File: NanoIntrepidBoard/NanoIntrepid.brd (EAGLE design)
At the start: 35 x 50 mm, 22 parts, among them Q1 TRANS_NPN, Q2 TRANS_NPN, Q3 TRANS_NPN, Q4 TRANS_PNP, Q5 TRANS_PNP, Q6 TRANS_PNP, U1 NANO, U2 MOSFET_P, U3 MOSFET_P, U4 MOSFET_P

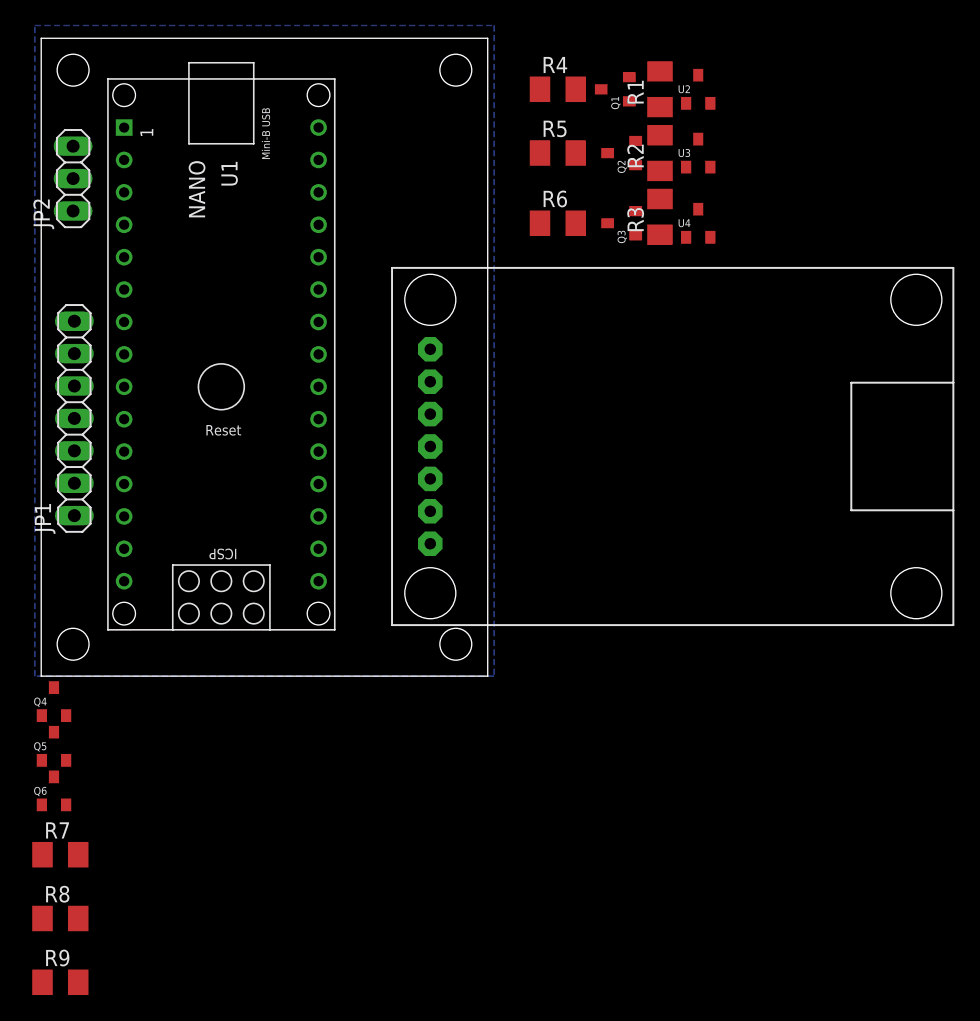
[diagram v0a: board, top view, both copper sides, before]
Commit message: Fixed some Eagle Library mistakes and started laying out board
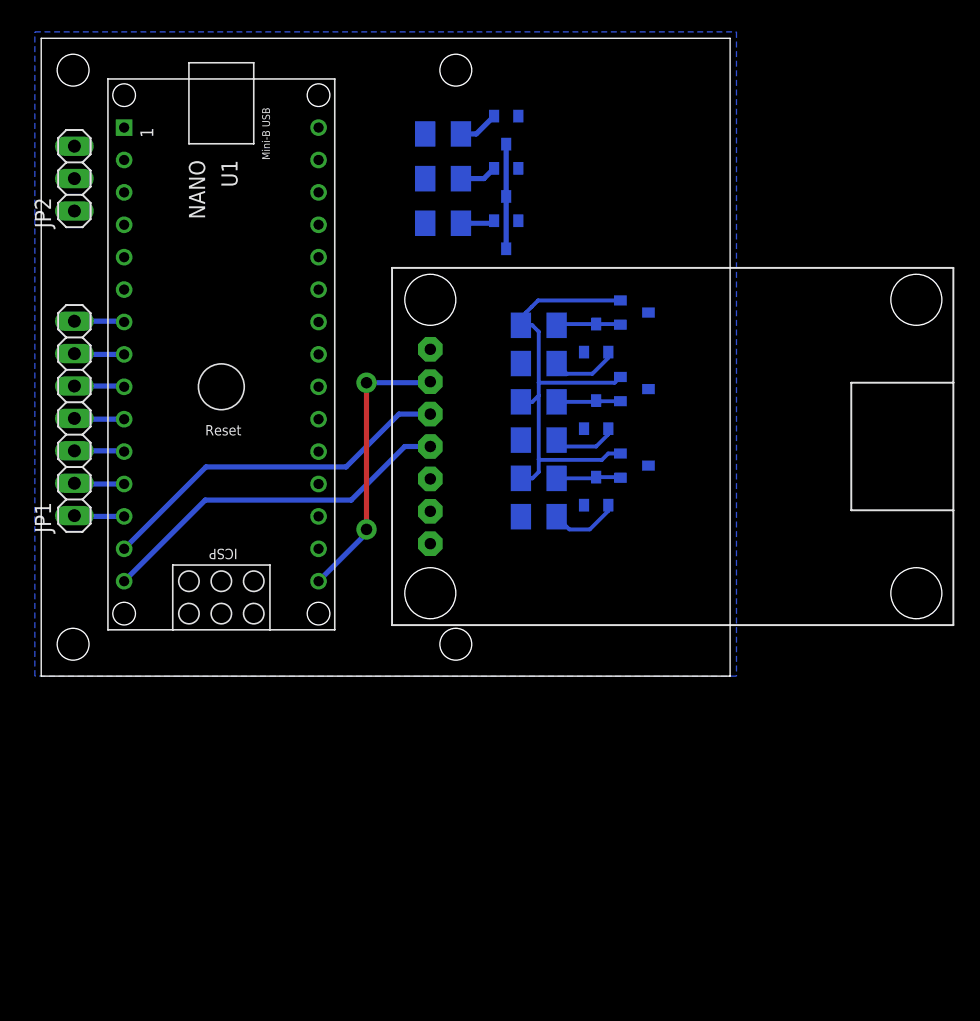
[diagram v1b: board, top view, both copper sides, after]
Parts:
- moved R9 66.6 mm to (31.5, 35.5), flipped to the bottom, turned to 180 degrees
- moved R8 65.3 mm to (31.5, 39.0), flipped to the bottom, turned to 180 degrees
- moved R7 64.0 mm to (31.5, 42.5), flipped to the bottom, turned to 180 degrees
- moved Q4 55.6 mm to (36.5, 41.8), flipped to the bottom, turned to 180 degrees
- moved Q5 55.1 mm to (36.5, 37.7), flipped to the bottom, turned to 180 degrees
- moved Q6 54.7 mm to (36.5, 33.6), flipped to the bottom, turned to 180 degrees
- moved R6 23.0 mm to (39.0, 12.5), flipped to the bottom, turned to 180 degrees
- moved R3 22.6 mm to (39.0, 15.5), flipped to the bottom, turned to 0 degrees
- moved R5 22.5 mm to (39.0, 18.5), flipped to the bottom, turned to 180 degrees
- moved R2 21.7 mm to (39.0, 21.5), flipped to the bottom, turned to 0 degrees
- moved R4 21.6 mm to (39.0, 24.5), flipped to the bottom, turned to 180 degrees
- moved R1 20.8 mm to (39.0, 27.5), flipped to the bottom, turned to 0 degrees
- moved U4 20.4 mm to (47.5, 16.5), flipped to the bottom, turned to 90 degrees
- moved Q3 20.0 mm to (43.5, 15.5), flipped to the bottom, turned to 0 degrees
- moved U3 19.9 mm to (47.5, 22.5), flipped to the bottom, turned to 90 degrees
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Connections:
- net +12V: now also U2.2, U3.2, U4.2; no longer U2.1, U3.1, U4.1
- net N$13: now also U2.1; no longer U2.2
- net N$14: now also U3.1; no longer U3.2
- net N$16: now also U4.1; no longer U4.2
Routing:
- net +12V: track 0.00 -> 38.1 mm
- net N$2: track 0.00 -> 28.4 mm
- net N$3: track 0.00 -> 28.4 mm
- net N$1: track 0.00 -> 22.2 mm, vias 0 -> 2
- net +5V: track 0.00 -> 8.20 mm
- net N$17: track 0.00 -> 5.51 mm
- net N$12: track 0.00 -> 5.35 mm
- net N$11: track 0.00 -> 5.10 mm
- net N$14: track 0.00 -> 5.09 mm
- net N$13: track 0.00 -> 5.06 mm
- net N$16: track 0.00 -> 5.06 mm
- net N$5: track 0.00 -> 3.92 mm
- net N$10: track 0.00 -> 3.92 mm
- net N$8: track 0.00 -> 3.92 mm
- net N$6: track 0.00 -> 3.92 mm
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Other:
- board size 35 x 50 mm -> 54 x 50 mm

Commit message: Worked on board files
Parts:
- added JP3: (no value), pinhead:1X01
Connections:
- new net ABS_UC: R8.1, U1.23
- new net AIRBAG_UC: R7.1, U1.24
- new net HB_UC: R4.1, U1.21
- new net LTURN_UC: R6.1, U1.19
- new net OIL_UC: R9.1, U1.22
- new net PB: JP3.1, U1.6
- new net RTURN_UC: R5.1, U1.20
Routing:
- net LTURN_UC: track 0.00 -> 43.7 mm, vias 0 -> 2
- net HB_UC: track 0.00 -> 20.6 mm
- net AIRBAG_UC: track 0.00 -> 20.0 mm
- net ABS_UC: track 0.00 -> 19.4 mm
- net RTURN_UC: track 0.00 -> 19.1 mm
- net OIL_UC: track 0.00 -> 16.9 mm
- net PB: track 0.00 -> 4.60 mm
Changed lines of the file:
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@@
 <?xml version="1.0" encoding="utf-8"?>
 <!DOCTYPE eagle SYSTEM "eagle.dtd">
-<eagle version="9.6.2">
+<eagle version="7.5.0">
 <drawing>
 <settings>
 <setting alwaysvectorfont="no"/>
-<setting keepoldvectorfont="yes"/>
 <setting verticaltext="up"/>
 </settings>
@@
 <param name="dpMaxLengthDifference" value="10mm"/>
 <param name="dpGapFactor" value="2.5"/>
+<param name="checkGrid" value="0"/>
 <param name="checkAngle" value="0"/>
 <param name="checkFont" value="1"/>
 <param name="checkRestrict" value="1"/>
-<param name="checkStop" value="0"/>
-<param name="checkValues" value="0"/>
-<param name="checkNames" value="1"/>
-<param name="checkWireStubs" value="1"/>
-<param name="checkPolygonWidth" value="0"/>
 <param name="useDiameter" value="13"/>
 <param name="maxErrors" value="50"/>
@@
 </element>
 <element name="B1" library="DR" package="MCP2515_BREAKOUT" value="MCP2515_BREAKOUT" x="30.5" y="18" smashed="yes"/>
-<element name="JP1" library="pinhead" library_urn="urn:adsk.eagle:library:325" package="1X07" package3d_urn="urn:adsk.eagle:package:22477/2" value="" x="2.6" y="20.2" smashed="yes" rot="R90">
+<element name="JP1" library="pinhead" package="1X07" value="" x="2.6" y="20.2" smashed="yes" rot="R90">
 <attribute name="NAME" x="0.7712" y="11.2338" size="1.27" layer="25" ratio="10" rot="R90"/>
 <attribute name="POPULARITY" value="0" x="2.6" y="20.2" size="1.778" layer="27" rot="R90" display="off"/>
 <attribute name="VALUE" x="5.775" y="11.31" size="1.27" layer="27" rot="R90"/>
 </element>
-<element name="JP2" library="pinhead" library_urn="urn:adsk.eagle:library:325" package="1X03" package3d_urn="urn:adsk.eagle:package:22458/2" value="" x="2.6" y="39" smashed="yes" rot="R90">
+<element name="JP2" library="pinhead" package="1X03" value="" x="2.6" y="39" smashed="yes" rot="R90">
 <attribute name="NAME" x="0.7712" y="35.1138" size="1.27" layer="25" ratio="10" rot="R90"/>
 <attribute name="POPULARITY" value="92" x="2.6" y="39" size="1.778" layer="27" rot="R90" display="off"/>
@@
 <attribute name="VALUE" x="30.23" y="38.04" size="1.27" layer="28" rot="MR180"/>
 </element>
+<element name="JP3" library="pinhead" package="1X01" value="" x="2.6" y="32"/>
 </elements>
 <signals>
@@
 <wire x1="45.4" y1="29.45" x2="38.95" y2="29.45" width="0.3048" layer="16"/>
 <wire x1="38.95" y1="29.45" x2="38.45" y2="28.95" width="0.3048" layer="16"/>
-<wire x1="2.6" y1="36.46" x2="37.6" y2="27.5" width="0" layer="19" extent="16-16"/>
+<wire x1="2.6" y1="36.46" x2="37.5" y2="28" width="0" layer="19" extent="16-16"/>
 </signal>
 <signal name="N$12">
@@
 <contactref element="U2" pad="3"/>
 </signal>
+<signal name="PB">
+<contactref element="U1" pad="6"/>
+<contactref element="JP3" pad="1"/>
+<wire x1="6.5" y1="30.3" x2="4.3" y2="30.3" width="0.4064" layer="16"/>
+<wire x1="4.3" y1="30.3" x2="2.6" y2="32" width="0.4064" layer="16"/>
+</signal>
+<signal name="LTURN_UC">
+<contactref element="U1" pad="19"/>
+<contactref element="R6" pad="1"/>
+<wire x1="21.74" y1="15.06" x2="17.06" y2="15.06" width="0.4064" layer="16"/>
+<wire x1="17.06" y1="15.06" x2="17" y2="15" width="0.4064" layer="16"/>
+<via x="17" y="15" extent="1-16" drill="0.9" diameter="1.6764" shape="octagon"/>
+<wire x1="17" y1="15" x2="17" y2="5" width="0.4064" layer="1"/>
+<wire x1="17" y1="5" x2="20.5" y2="1.5" width="0.4064" layer="1"/>
+<wire x1="20.5" y1="1.5" x2="30.5" y2="1.5" width="0.4064" layer="1"/>
+<wire x1="30.5" y1="1.5" x2="35.5" y2="6.5" width="0.4064" layer="1"/>
+<via x="35.5" y="6.5" extent="1-16" drill="0.9" diameter="1.6764" shape="octagon"/>
+<wire x1="35.5" y1="6.5" x2="35.5" y2="10.4" width="0.4064" layer="16"/>
+<wire x1="35.5" y1="10.4" x2="37.6" y2="12.5" width="0.4064" layer="16"/>
+</signal>
+<signal name="RTURN_UC">
+<contactref element="U1" pad="20"/>
+<contactref element="R5" pad="1"/>
+<wire x1="21.74" y1="17.6" x2="23.6" y2="17.6" width="0.4064" layer="16"/>
+<wire x1="23.6" y1="17.6" x2="28" y2="22" width="0.4064" layer="16"/>
+<wire x1="28" y1="22" x2="29.3" y2="22" width="0.254" layer="16"/>
+<wire x1="29.3" y1="22" x2="29.5" y2="21.8" width="0.254" layer="16"/>
+<wire x1="29.5" y1="21.8" x2="33.4" y2="21.8" width="0.254" layer="16"/>
+<wire x1="33.4" y1="21.8" x2="36.7" y2="18.5" width="0.254" layer="16"/>
+<wire x1="36.7" y1="18.5" x2="37.6" y2="18.5" width="0.254" layer="16"/>
+</signal>
+<signal name="HB_UC">
+<contactref element="U1" pad="21"/>
+<contactref element="R4" pad="1"/>
+<wire x1="21.74" y1="20.14" x2="22.14" y2="20.14" width="0.4064" layer="16"/>
+<wire x1="22.14" y1="20.14" x2="24" y2="22" width="0.4064" layer="16"/>
+<wire x1="24" y1="22" x2="24" y2="23.5" width="0.4064" layer="16"/>
+<wire x1="24" y1="23.5" x2="27.5" y2="27" width="0.4064" layer="16"/>
+<wire x1="27.5" y1="27" x2="35.1" y2="27" width="0.4064" layer="16"/>
+<wire x1="35.1" y1="27" x2="37.6" y2="24.5" width="0.4064" layer="16"/>
+</signal>
+<signal name="OIL_UC">
+<contactref element="U1" pad="22"/>
+<contactref element="R9" pad="1"/>
+<wire x1="21.74" y1="22.68" x2="21.74" y2="22.74" width="0.4064" layer="16"/>
+<wire x1="21.74" y1="22.74" x2="26" y2="27" width="0.4064" layer="16"/>
+<wire x1="26" y1="27" x2="26" y2="32.5" width="0.4064" layer="16"/>
+<wire x1="26" y1="32.5" x2="29" y2="35.5" width="0.4064" layer="16"/>
+<wire x1="29" y1="35.5" x2="30.1" y2="35.5" width="0.4064" layer="16"/>
+</signal>
+<signal name="ABS_UC">
+<contactref element="U1" pad="23"/>
+<contactref element="R8" pad="1"/>
+<wire x1="21.74" y1="25.22" x2="21.74" y2="25.24" width="0.4064" layer="16"/>
+<wire x1="21.74" y1="25.24" x2="25" y2="28.5" width="0.4064" layer="16"/>
+<wire x1="25" y1="28.5" x2="25" y2="37.5" width="0.4064" layer="16"/>
+<wire x1="25" y1="37.5" x2="26.5" y2="39" width="0.4064" layer="16"/>
+<wire x1="26.5" y1="39" x2="30.1" y2="39" width="0.4064" layer="16"/>
+</signal>
+<signal name="AIRBAG_UC">
+<contactref element="U1" pad="24"/>
+<contactref element="R7" pad="1"/>
+<wire x1="21.74" y1="27.76" x2="21.76" y2="27.76" width="0.4064" layer="16"/>
+<wire x1="21.76" y1="27.76" x2="24" y2="30" width="0.4064" layer="16"/>
+<wire x1="24" y1="30" x2="24" y2="39.5" width="0.4064" layer="16"/>
+<wire x1="24" y1="39.5" x2="27" y2="42.5" width="0.4064" layer="16"/>
+<wire x1="27" y1="42.5" x2="30.1" y2="42.5" width="0.4064" layer="16"/>
+</signal>
 </signals>
-<mfgpreviewcolors>
-<mfgpreviewcolor name="soldermaskcolor" color="0xC8008000"/>
-<mfgpreviewcolor name="silkscreencolor" color="0xFFFEFEFE"/>
-<mfgpreviewcolor name="backgroundcolor" color="0xFF282828"/>
-<mfgpreviewcolor name="coppercolor" color="0xFFFFBF00"/>
-<mfgpreviewcolor name="substratecolor" color="0xFF786E46"/>
-</mfgpreviewcolors>
 <errors>
 </errors>
 </board>
 </drawing>
-<compatibility>
-<note version="8.2" severity="warning">
-Since Version 8.2, EAGLE supports online libraries. The ids
-of those online libraries will not be understood (or retained)
-with this version.
-</note>
-<note version="8.3" severity="warning">
-Since Version 8.3, EAGLE supports URNs for individual library
-assets (packages, symbols, and devices). The URNs of those assets
-will not be understood (or retained) with this version.
-</note>
-<note version="8.3" severity="warning">
-Since Version 8.3, EAGLE supports the association of 3D packages
-with devices in libraries, schematics, and board files. Those 3D
-packages will not be understood (or retained) with this version.
-</note>
-</compatibility>
 </eagle>

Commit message: Finishing board file
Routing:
- net +5V: track 8.20 -> 73.8 mm, vias 0 -> 2
- net +12V: track 38.1 -> 87.9 mm, vias 0 -> 4
- added copper zone on layer 1, net GND
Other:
- board size 54 x 50 mm -> 50 x 50 mm
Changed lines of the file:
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@@
 <?xml version="1.0" encoding="utf-8"?>
 <!DOCTYPE eagle SYSTEM "eagle.dtd">
-<eagle version="7.5.0">
+<eagle version="9.6.2">
 <drawing>
 <settings>
 <setting alwaysvectorfont="no"/>
+<setting keepoldvectorfont="yes"/>
 <setting verticaltext="up"/>
 </settings>
@@
 <board>
 <plain>
-<wire x1="0" y1="0" x2="54" y2="0" width="0" layer="20"/>
-<wire x1="54" y1="0" x2="54" y2="50" width="0" layer="20"/>
-<wire x1="54" y1="50" x2="0" y2="50" width="0" layer="20"/>
+<wire x1="0" y1="0" x2="50" y2="0" width="0" layer="20"/>
+<wire x1="50" y1="0" x2="50" y2="50" width="0" layer="20"/>
+<wire x1="50" y1="50" x2="0" y2="50" width="0" layer="20"/>
 <wire x1="0" y1="50" x2="0" y2="0" width="0" layer="20"/>
 <hole x="2.5" y="2.5" drill="2.5"/>
 <hole x="2.5" y="47.5" drill="2.5"/>
-<hole x="32.5" y="2.5" drill="2.5"/>
-<hole x="32.5" y="47.5" drill="2.5"/>
+<hole x="47" y="1.5" drill="2.5"/>
+<hole x="47.5" y="47.5" drill="2.5"/>
 </plain>
 <attributes>
@@
 <param name="dpMaxLengthDifference" value="10mm"/>
 <param name="dpGapFactor" value="2.5"/>
-<param name="checkGrid" value="0"/>
 <param name="checkAngle" value="0"/>
 <param name="checkFont" value="1"/>
 <param name="checkRestrict" value="1"/>
+<param name="checkStop" value="0"/>
+<param name="checkValues" value="0"/>
+<param name="checkNames" value="1"/>
+<param name="checkWireStubs" value="1"/>
+<param name="checkPolygonWidth" value="0"/>
 <param name="useDiameter" value="13"/>
 <param name="maxErrors" value="50"/>
@@
 <attribute name="VALUE" x="30.23" y="38.04" size="1.27" layer="28" rot="MR180"/>
 </element>
-<element name="JP3" library="pinhead" package="1X01" value="" x="2.6" y="32"/>
+<element name="JP3" library="pinhead" package="1X01" value="" x="2.6" y="32" smashed="yes">
+<attribute name="NAME" x="1.2538" y="33.8288" size="1.27" layer="25" ratio="10"/>
+<attribute name="VALUE" x="1.33" y="28.825" size="1.27" layer="27"/>
+</element>
 </elements>
 <signals>
 <signal name="GND">
-<polygon width="0.1524" layer="16" isolate="0.4064">
+<polygon width="0.1524" layer="16" isolate="0.5">
 <vertex x="-0.5" y="50.5"/>
 <vertex x="54.5" y="50.5"/>
@@
 <contactref element="Q2" pad="2"/>
 <contactref element="Q3" pad="2"/>
+<polygon width="0.3048" layer="1" isolate="0.6096">
+<vertex x="-1" y="50.5"/>
+<vertex x="51" y="50.5"/>
+<vertex x="51" y="-0.5"/>
+<vertex x="-1" y="-0.5"/>
+</polygon>
 </signal>
 <signal name="5V">
@@
 <contactref element="U1" pad="15"/>
 <contactref element="B1" pad="4"/>
-<wire x1="6.5" y1="7.44" x2="12.86" y2="13.8" width="0.4064" layer="16"/>
-<wire x1="24.3" y1="13.8" x2="28.5" y2="18" width="0.4064" layer="16"/>
+<wire x1="28.5" y1="18" x2="24.3" y2="13.8" width="0.4064" layer="16"/>
 <wire x1="28.5" y1="18" x2="30.5" y2="18" width="0.4064" layer="16"/>
-<wire x1="12.86" y1="13.8" x2="24.3" y2="13.8" width="0.4064" layer="16"/>
+<wire x1="18" y1="12.5" x2="11.5" y2="12.5" width="0.4064" layer="16"/>
+<wire x1="11.5" y1="12.5" x2="6.5" y2="7.5" width="0.4064" layer="16"/>
+<wire x1="6.5" y1="7.5" x2="6.5" y2="7.44" width="0.4064" layer="16"/>
+<wire x1="24.3" y1="13.8" x2="19.3" y2="13.8" width="0.4064" layer="16"/>
+<wire x1="19.3" y1="13.8" x2="18" y2="12.5" width="0.4064" layer="16"/>
 </signal>
 <signal name="N$3">
@@
 <wire x1="36.45" y1="41.7" x2="36.45" y2="37.6" width="0.4064" layer="16"/>
 <wire x1="36.45" y1="37.6" x2="36.45" y2="33.5" width="0.4064" layer="16"/>
-<wire x1="30.5" y1="10.38" x2="36.45" y2="33.5" width="0" layer="19" extent="16-16"/>
-<wire x1="2.6" y1="39" x2="36.45" y2="37.6" width="0" layer="19" extent="16-16"/>
+<wire x1="30.5" y1="10.38" x2="32.38" y2="10.38" width="0.254" layer="16"/>
+<wire x1="32.38" y1="10.38" x2="35" y2="13" width="0.254" layer="16"/>
+<via x="35" y="13" extent="1-16" drill="0.9" diameter="1.6"/>
+<wire x1="35" y1="13" x2="38.5" y2="16.5" width="0.4064" layer="1"/>
+<wire x1="38.5" y1="28.5" x2="38.5" y2="16.5" width="0.4064" layer="1"/>
+<via x="36" y="31" extent="1-16" drill="0.9" diameter="1.6"/>
+<wire x1="38.5" y1="28.5" x2="36" y2="31" width="0.4064" layer="1"/>
+<wire x1="36" y1="31" x2="36.45" y2="31.45" width="0.3048" layer="16"/>
+<wire x1="36.45" y1="31.45" x2="36.45" y2="33.5" width="0.3048" layer="16"/>
+<wire x1="2.6" y1="39" x2="2.8" y2="39.2" width="0.3048" layer="1"/>
+<wire x1="27.8" y1="39.2" x2="36" y2="31" width="0.4064" layer="1"/>
+<wire x1="2.8" y1="39.2" x2="27.8" y2="39.2" width="0.4064" layer="1"/>
 </signal>
 <signal name="N$4">
@@
 <contactref element="U2" pad="2"/>
 <wire x1="37.6" y1="27.5" x2="38.5" y2="27.5" width="0.3048" layer="16"/>
-<wire x1="38.5" y1="27.5" x2="39" y2="27" width="0.3048" layer="16"/>
-<wire x1="39" y1="27" x2="39" y2="23" width="0.3048" layer="16"/>
 <wire x1="39" y1="23" x2="39" y2="22" width="0.3048" layer="16"/>
 <wire x1="39" y1="22" x2="38.5" y2="21.5" width="0.3048" layer="16"/>
 <wire x1="38.5" y1="21.5" x2="37.6" y2="21.5" width="0.3048" layer="16"/>
 <wire x1="37.6" y1="15.5" x2="38.5" y2="15.5" width="0.3048" layer="16"/>
-<wire x1="38.5" y1="15.5" x2="39" y2="16" width="0.3048" layer="16"/>
-<wire x1="39" y1="16" x2="39" y2="17" width="0.3048" layer="16"/>
-<wire x1="39" y1="17" x2="39" y2="22" width="0.3048" layer="16"/>
-<wire x1="38.45" y1="28.95" x2="38" y2="28.5" width="0.3048" layer="16"/>
-<wire x1="38" y1="28.5" x2="37.5" y2="28" width="0.3048" layer="16"/>
+<wire x1="38.95" y1="29.45" x2="37.5" y2="28" width="0.3048" layer="16"/>
 <wire x1="37.5" y1="28" x2="37.5" y2="27.6" width="0.3048" layer="16"/>
 <wire x1="37.5" y1="27.6" x2="37.6" y2="27.5" width="0.3048" layer="16"/>
@@
 <wire x1="44.45" y1="17.45" x2="43.95" y2="16.95" width="0.3048" layer="16"/>
 <wire x1="45.4" y1="29.45" x2="38.95" y2="29.45" width="0.3048" layer="16"/>
-<wire x1="38.95" y1="29.45" x2="38.45" y2="28.95" width="0.3048" layer="16"/>
-<wire x1="2.6" y1="36.46" x2="37.5" y2="28" width="0" layer="19" extent="16-16"/>
+<wire x1="2.6" y1="36.46" x2="5.06" y2="36.46" width="0.4064" layer="1"/>
+<wire x1="5.06" y1="36.46" x2="5.3" y2="36.7" width="0.4064" layer="1"/>
+<wire x1="33.6684" y1="30.8124" x2="33.6684" y2="29.3316" width="0.4064" layer="1"/>
+<wire x1="33.6684" y1="29.3316" x2="34.5" y2="28.5" width="0.4064" layer="1"/>
+<wire x1="5.3" y1="36.7" x2="27.7808" y2="36.7" width="0.4064" layer="1"/>
+<wire x1="27.7808" y1="36.7" x2="33.6684" y2="30.8124" width="0.4064" layer="1"/>
+<wire x1="37.6" y1="27.5" x2="36.6" y2="28.5" width="0.4064" layer="16"/>
+<wire x1="36.6" y1="28.5" x2="34.5" y2="28.5" width="0.4064" layer="16"/>
+<via x="34.5" y="28.5" extent="1-16" drill="0.9" diameter="1.6"/>
+<wire x1="38.5" y1="15.5" x2="39.05" y2="16.05" width="0.4064" layer="16"/>
+<wire x1="39.05" y1="16.05" x2="39.05" y2="16.95" width="0.4064" layer="16"/>
+<wire x1="45.4" y1="29.45" x2="45.4" y2="30.4" width="0.3048" layer="16"/>
+<wire x1="45.4" y1="30.4" x2="46" y2="31" width="0.3048" layer="16"/>
+<wire x1="46" y1="31" x2="46" y2="31.5" width="0.3048" layer="16"/>
+<via x="46" y="31.5" extent="1-16" drill="0.9" diameter="1.6"/>
+<wire x1="46" y1="31.5" x2="47" y2="30.5" width="0.3048" layer="1"/>
+<wire x1="47" y1="30.5" x2="47" y2="25.5" width="0.3048" layer="1"/>
+<via x="47" y="19" extent="1-16" drill="0.9" diameter="1.6"/>
+<wire x1="47" y1="25" x2="47" y2="19" width="0.3048" layer="1"/>
+<wire x1="47" y1="19" x2="45.45" y2="17.45" width="0.3048" layer="16"/>
+<wire x1="45.45" y1="17.45" x2="45.4" y2="17.45" width="0.3048" layer="16"/>
+<wire x1="45.4" y1="23.45" x2="46.95" y2="25" width="0.3048" layer="16"/>
+<wire x1="46.95" y1="25" x2="47" y2="25" width="0.3048" layer="16"/>
+<via x="47" y="25" extent="1-16" drill="0.9" diameter="1.6"/>
+<wire x1="47" y1="25" x2="47" y2="25.5" width="0.3048" layer="1"/>
 </signal>
 <signal name="N$12">
@@
 </signal>
 </signals>
-<errors>
-</errors>
+<mfgpreviewcolors>
+<mfgpreviewcolor name="soldermaskcolor" color="0xC8008000"/>
+<mfgpreviewcolor name="silkscreencolor" color="0xFFFEFEFE"/>
+<mfgpreviewcolor name="backgroundcolor" color="0xFF282828"/>
+<mfgpreviewcolor name="coppercolor" color="0xFFFFBF00"/>
+<mfgpreviewcolor name="substratecolor" color="0xFF786E46"/>
+</mfgpreviewcolors>
 </board>
 </drawing>
